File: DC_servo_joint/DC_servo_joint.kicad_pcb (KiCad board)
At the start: 2 copper layers, 58.5 x 50 mm, 55 parts, among them U1 AS5600, U2 ESP32-C3-WROOM-02, U3 SP3485EN, U5 TPS563200

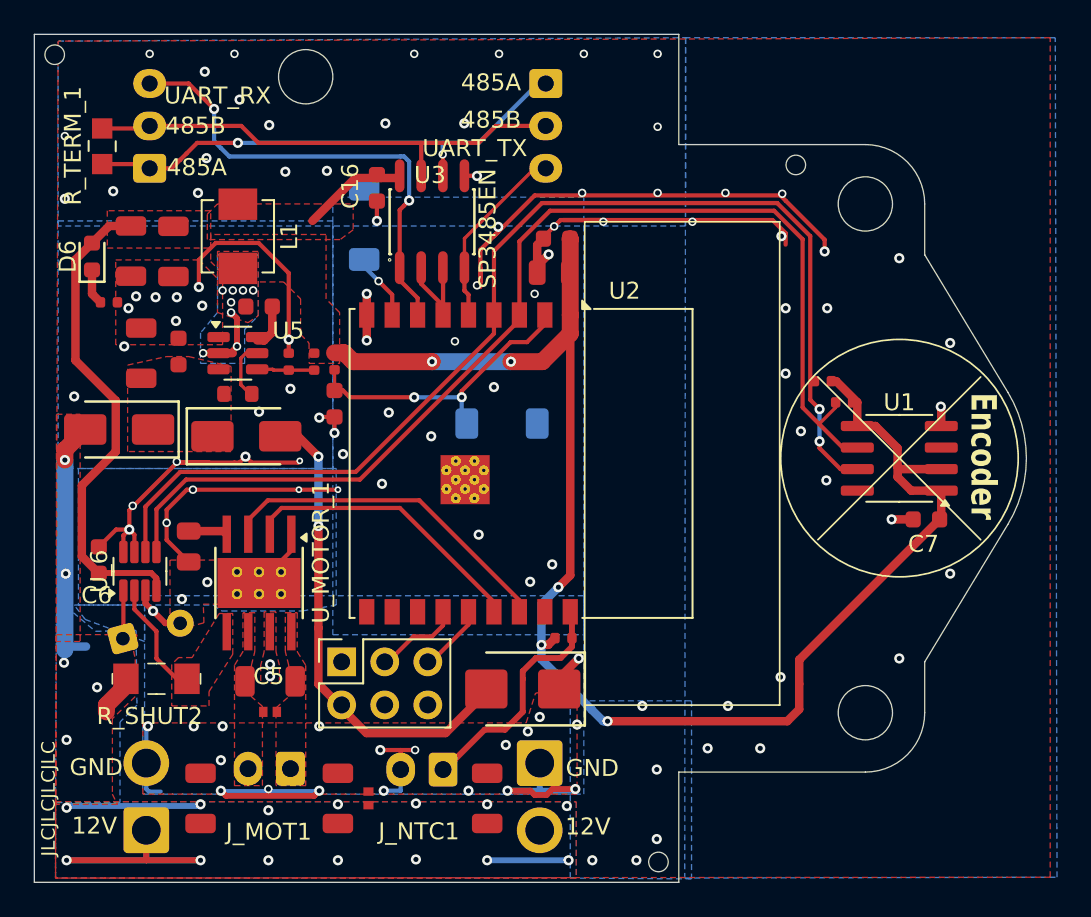
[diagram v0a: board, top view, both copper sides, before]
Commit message: Move GPIO2 to 3, Clean up I2C trace under encoder.
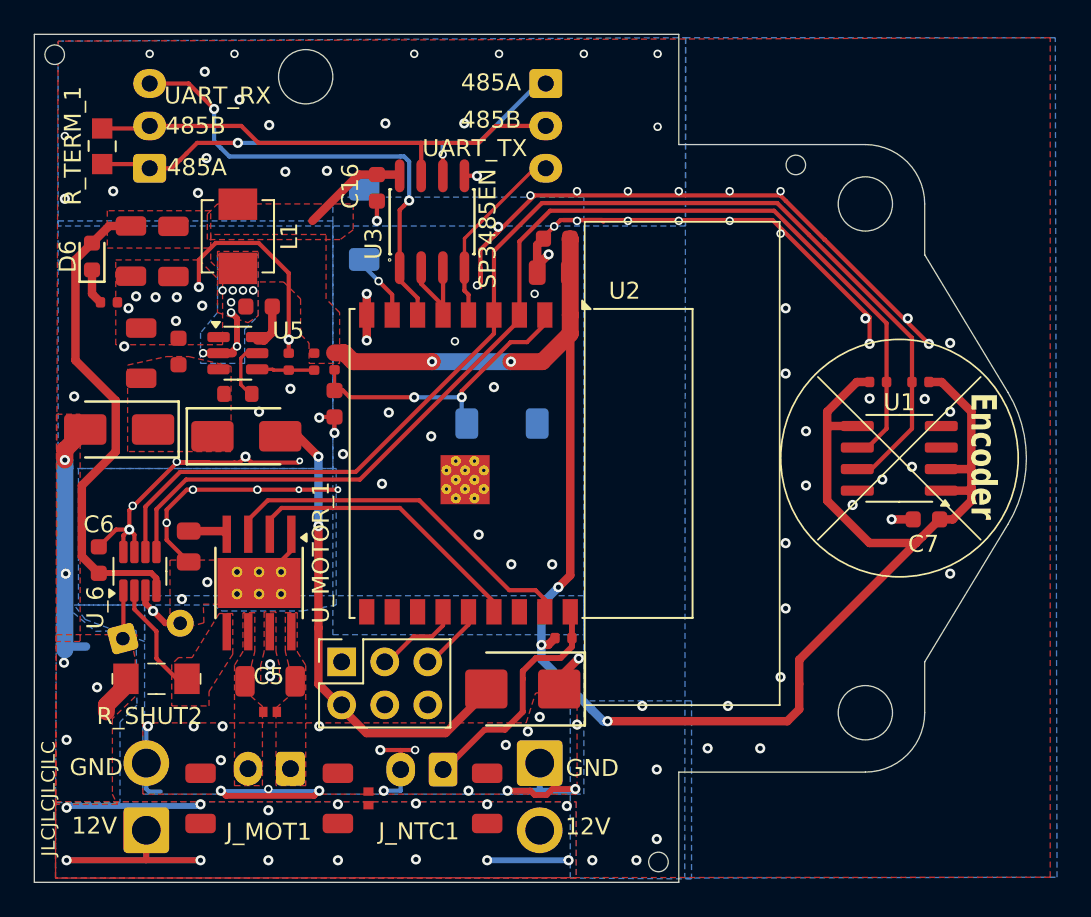
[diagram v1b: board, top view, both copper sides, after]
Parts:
- moved R_i2c2 5.75 mm to (151.2, 70.5)
- moved R_i2c1 2.33 mm to (148.8, 70.5), turned to 0 degrees
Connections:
- U2 pad 16: /pwm1_io2 -> unconnected-(U2-IO2-Pad16)
- U2 pad 17: unconnected-(U2-IO1-Pad17) -> /pwm1_io2
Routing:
- net +3.3V: track 124.5 -> 140.5 mm
- net GND: track 144.9 -> 159.6 mm, vias 112 -> 124
- net /SDA: track 68.2 -> 70.0 mm, vias 2 -> 0
- net /pwm1_io2: track 19.6 -> 21.1 mm
- net /SCL: track 66.8 -> 65.8 mm

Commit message: Save the final production run of the circuit. mistake on AS5600 pinout
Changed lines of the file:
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@@
 		(sheetname "/")
 		(sheetfile "DC_servo_joint.kicad_sch")
+		(attr exclude_from_bom)
 		(fp_text user "${REFERENCE}"
 			(at 0 2.5 0)
@@
 		(tags "SOT TO_SOT_SMD")
 		(property "Reference" "U_6"
-			(at -2.1375 -2.625 90)
+			(at 2.8625 -0.15 180)
 			(layer "F.SilkS")
 			(effects
@@
 		(sheetname "/")
 		(sheetfile "DC_servo_joint.kicad_sch")
+		(attr exclude_from_bom)
 		(fp_text user "${REFERENCE}"
 			(at 0 2.5 0)
@@
 			)
 		)
+		(property "FT Rotation Offset" "90"
+			(at 0 0 0)
+			(unlocked yes)
+			(layer "F.Fab")
+			(hide yes)
+			(effects
+				(font
+					(size 1 1)
+					(thickness 0.15)
+				)
+			)
+		)
 		(sheetname "/")
 		(sheetfile "DC_servo_joint.kicad_sch")
@@
 			)
 		)
+		(property "FT Rotation Offset" "-90"
+			(at 0 0 270)
+			(unlocked yes)
+			(layer "F.Fab")
+			(hide yes)
+			(effects
+				(font
+					(size 1 1)
+					(thickness 0.15)
+				)
+			)
+		)
 		(property ki_fp_filters "Texas*HTSOP*1EP*3.9x4.9mm*P1.27mm*EP2.95x4.9mm*Mask2.4x3.1mm*")
 		(sheetname "/")
@@
 		(sheetname "/")
 		(sheetfile "DC_servo_joint.kicad_sch")
+		(attr exclude_from_bom)
 		(fp_text user "${REFERENCE}"
 			(at 0 2.5 0)
@@
 		(tags "capacitor")
 		(property "Reference" "C6"
-			(at 2.1 0 0)
+			(at 0.4 -1.325 90)
 			(layer "F.SilkS")
 			(effects
